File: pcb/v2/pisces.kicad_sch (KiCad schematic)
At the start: 55 parts

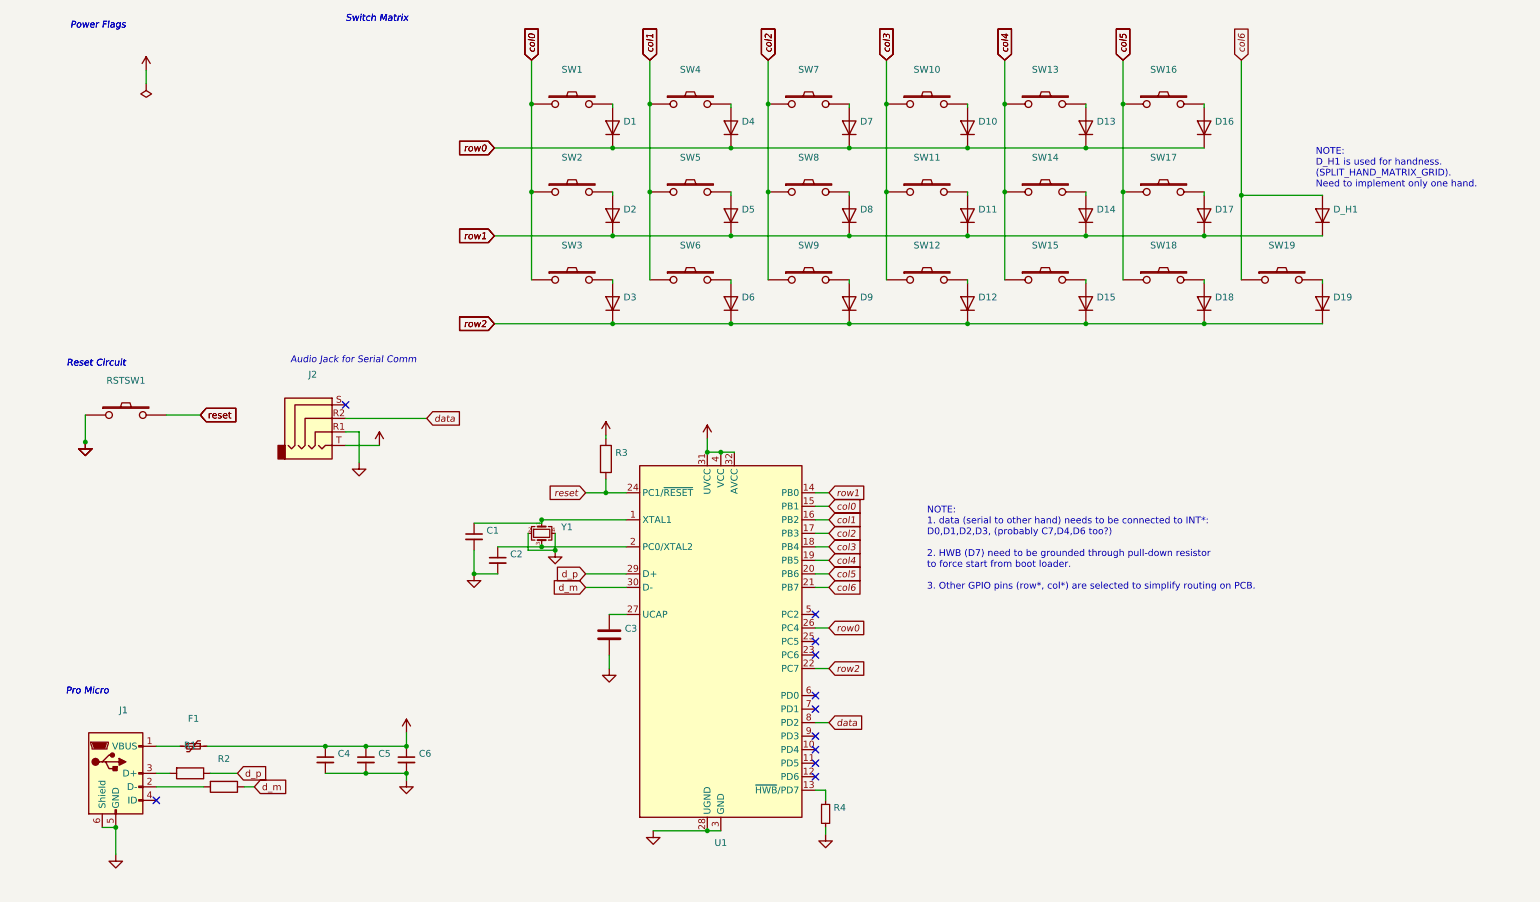
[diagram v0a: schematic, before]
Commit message: Removed ERC errors as many as possible
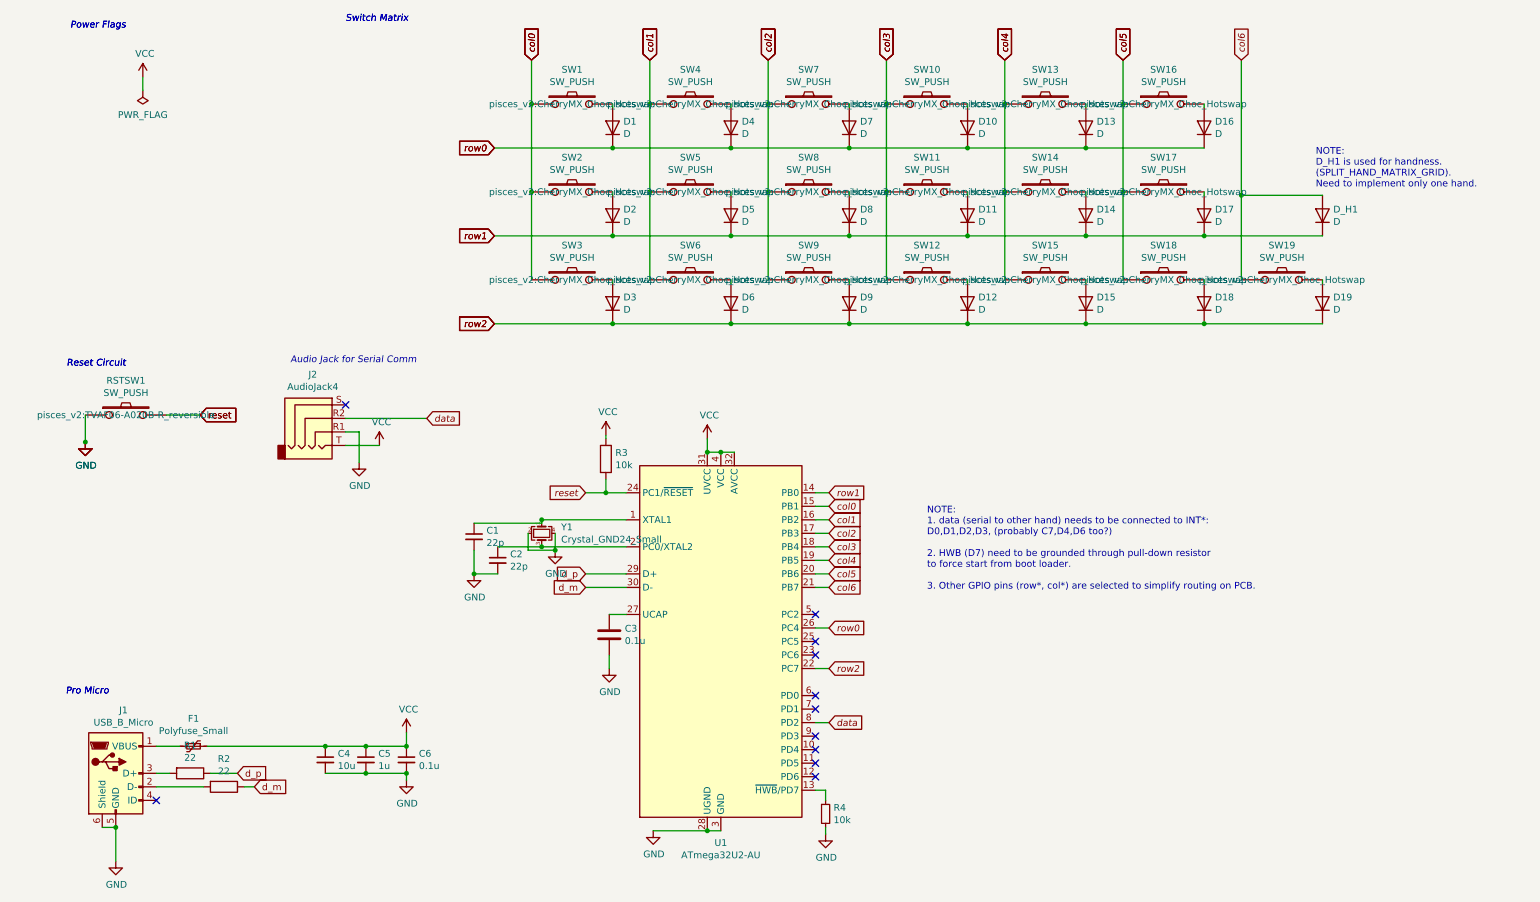
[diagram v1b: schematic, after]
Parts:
- C1, C2: value (none) -> 22p; footprint (none) -> Capacitor_SMD:C_0402_1005Metric; symbol pisces-rescue:C_Small-Device -> Device:C_Small
- C3: value (none) -> 0.1u; footprint (none) -> Capacitor_SMD:C_0402_1005Metric; symbol pisces-rescue:C-Device -> Device:C
- C4: value (none) -> 10u; footprint (none) -> Capacitor_SMD:C_0805_2012Metric; symbol pisces-rescue:C_Small-Device -> Device:C_Small
- C5: value (none) -> 1u; footprint (none) -> Capacitor_SMD:C_0603_1608Metric; symbol pisces-rescue:C_Small-Device -> Device:C_Small
- C6: value (none) -> 0.1u; footprint (none) -> Capacitor_SMD:C_0402_1005Metric; symbol pisces-rescue:C_Small-Device -> Device:C_Small
- D1, D10, D11, D12, D13, D14, D15, D16, D17, D18, D19, D2, D3, D4, D5, D6, D7, D8, D9, D_H1: value (none) -> D; footprint (none) -> pisces_v2:D3_SMD; symbol pisces-rescue:D-Device -> Device:D
- F1: value (none) -> Polyfuse_Small; footprint (none) -> pisces_v2:RESC1206X70N; symbol pisces-rescue:Polyfuse_Small-Device -> Device:Polyfuse_Small
- J1: value (none) -> USB_B_Micro; footprint (none) -> pisces_v2:HRS_ZX62R-B-5P; symbol pisces-rescue:USB_B_Micro-Connector -> Connector:USB_B_Micro
- J2: value (none) -> AudioJack4; footprint (none) -> pisces_v2:Jack_3.5mm_PJ320D_Horizontal_reversible; symbol pisces-rescue:AudioJack4-Connector -> Connector_Audio:AudioJack4
- R1, R2: value (none) -> 22; footprint (none) -> Resistor_SMD:R_0603_1608Metric; symbol pisces-rescue:R-Device -> Device:R
- R3: value (none) -> 10k; footprint (none) -> Resistor_SMD:R_0603_1608Metric; symbol pisces-rescue:R-Device -> Device:R
- R4: value (none) -> 10k; footprint (none) -> Resistor_SMD:R_0603_1608Metric; symbol pisces-rescue:R_Small-Device -> Device:R_Small
- RSTSW1: value (none) -> SW_PUSH; footprint (none) -> pisces_v2:TVAF06-A020B-R_reversible; symbol pisces-rescue:SW_PUSH-kbd -> kbd:SW_PUSH
- SW1, SW10, SW11, SW12, SW13, SW14, SW15, SW16, SW17, SW18, SW19, SW2, SW3, SW4, SW5, SW6, SW7, SW8, SW9: value (none) -> SW_PUSH; footprint (none) -> pisces_v2:CherryMX_Choc_Hotswap; symbol pisces-rescue:SW_PUSH-kbd -> kbd:SW_PUSH
- U1: value (none) -> ATmega32U2-AU; footprint (none) -> Package_QFP:TQFP-32_7x7mm_P0.8mm; symbol pisces-rescue:ATmega32U2-AU-MCU_Microchip_ATmega -> MCU_Microchip_ATmega:ATmega32U2-A
- Y1: value (none) -> Crystal_GND24_Small; footprint (none) -> Crystal:Crystal_SMD_SeikoEpson_FA238-4Pin_3.2x2.5mm; symbol pisces-rescue:Crystal_GND24_Small-Device -> Device:Crystal_GND24_Small
